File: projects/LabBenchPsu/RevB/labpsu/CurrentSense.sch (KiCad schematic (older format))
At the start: 24 parts

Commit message: working on schematic
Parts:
- added C21: 100nF, symbol C
- added R36: 1K, symbol R
- gave numbers to parts that had none: 23
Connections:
- net CurrentSense: now also C21.1, R36.1; no longer IC2.7 (OUT), R35.1
- net GND: now also C21.2
- new net: IC2.7 (OUT), R35.1, R36.2
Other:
- note added: "1mV / 1mA"
- note added: "Currents up to 320mA can be measured with high\nprecision through the INA219. For higher currents\nthe semi-precisese differential amplifier can be used."
- note added: "Differential amplifier high-side current sensor"
- note added: "differential amplifier"
- note added: "voltage follower"

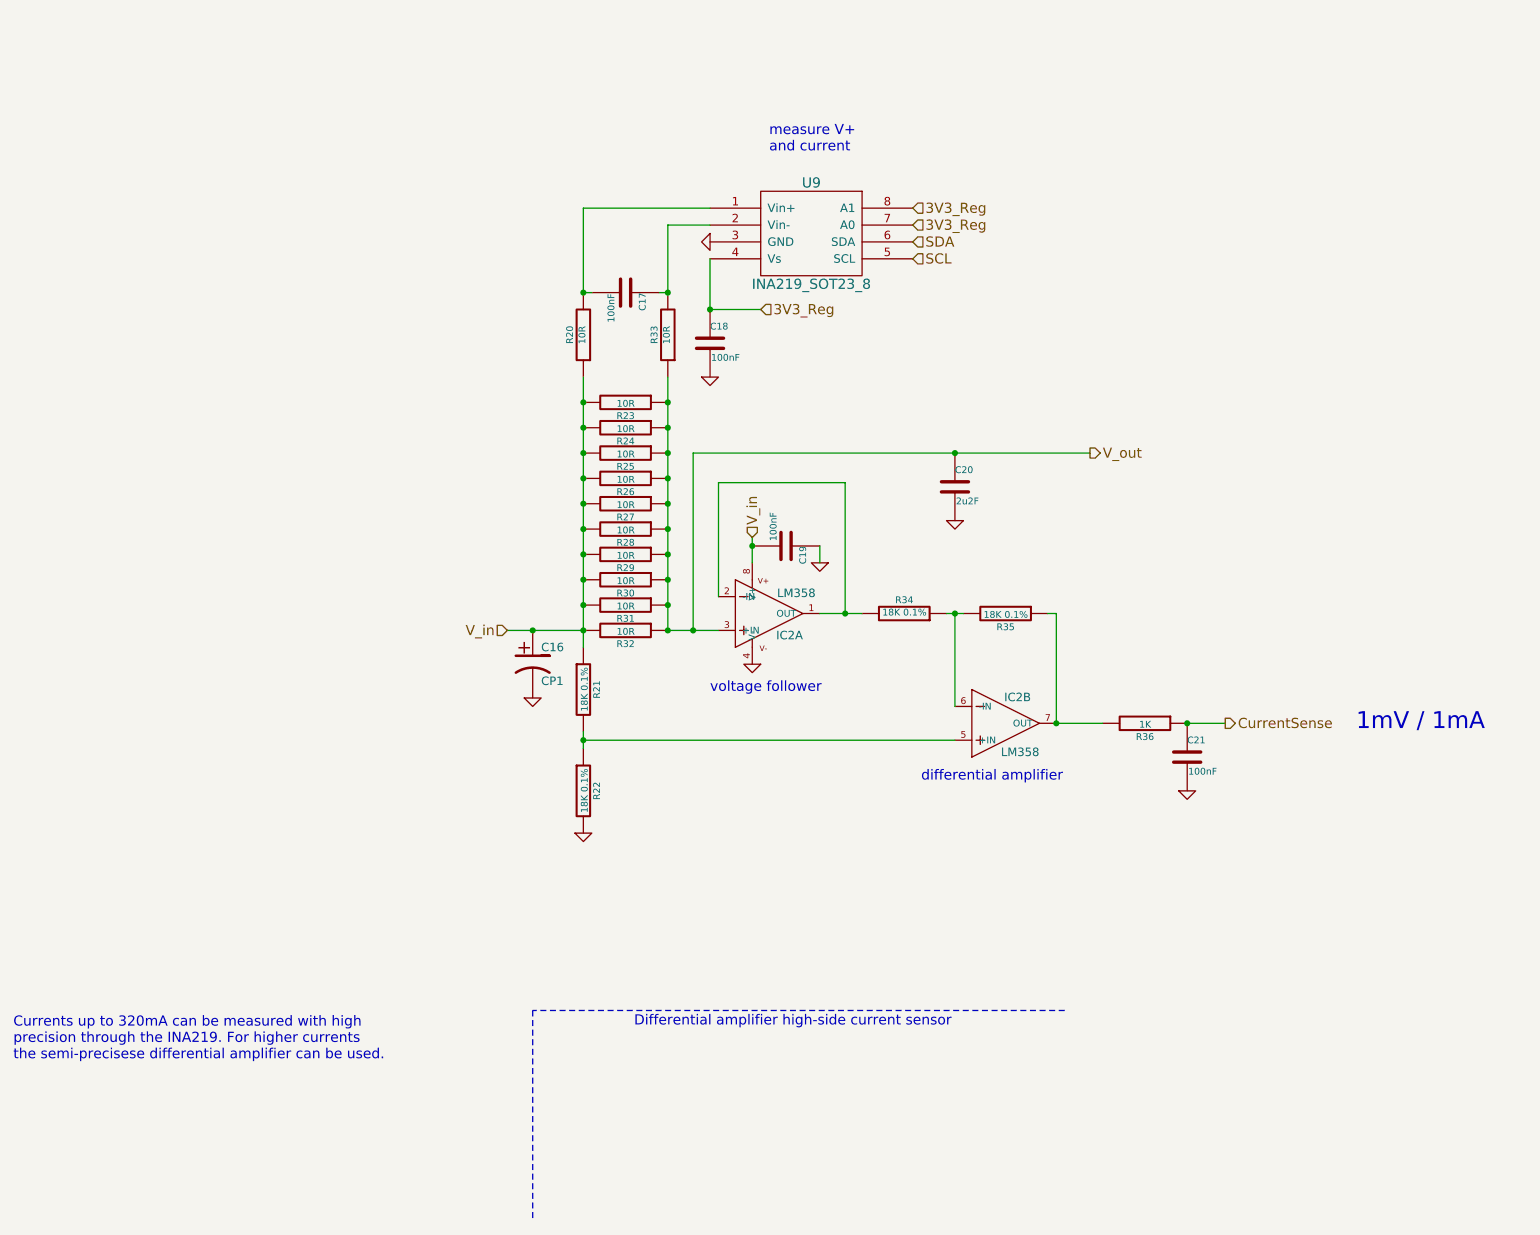
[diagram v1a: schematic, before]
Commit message: redraw schematic
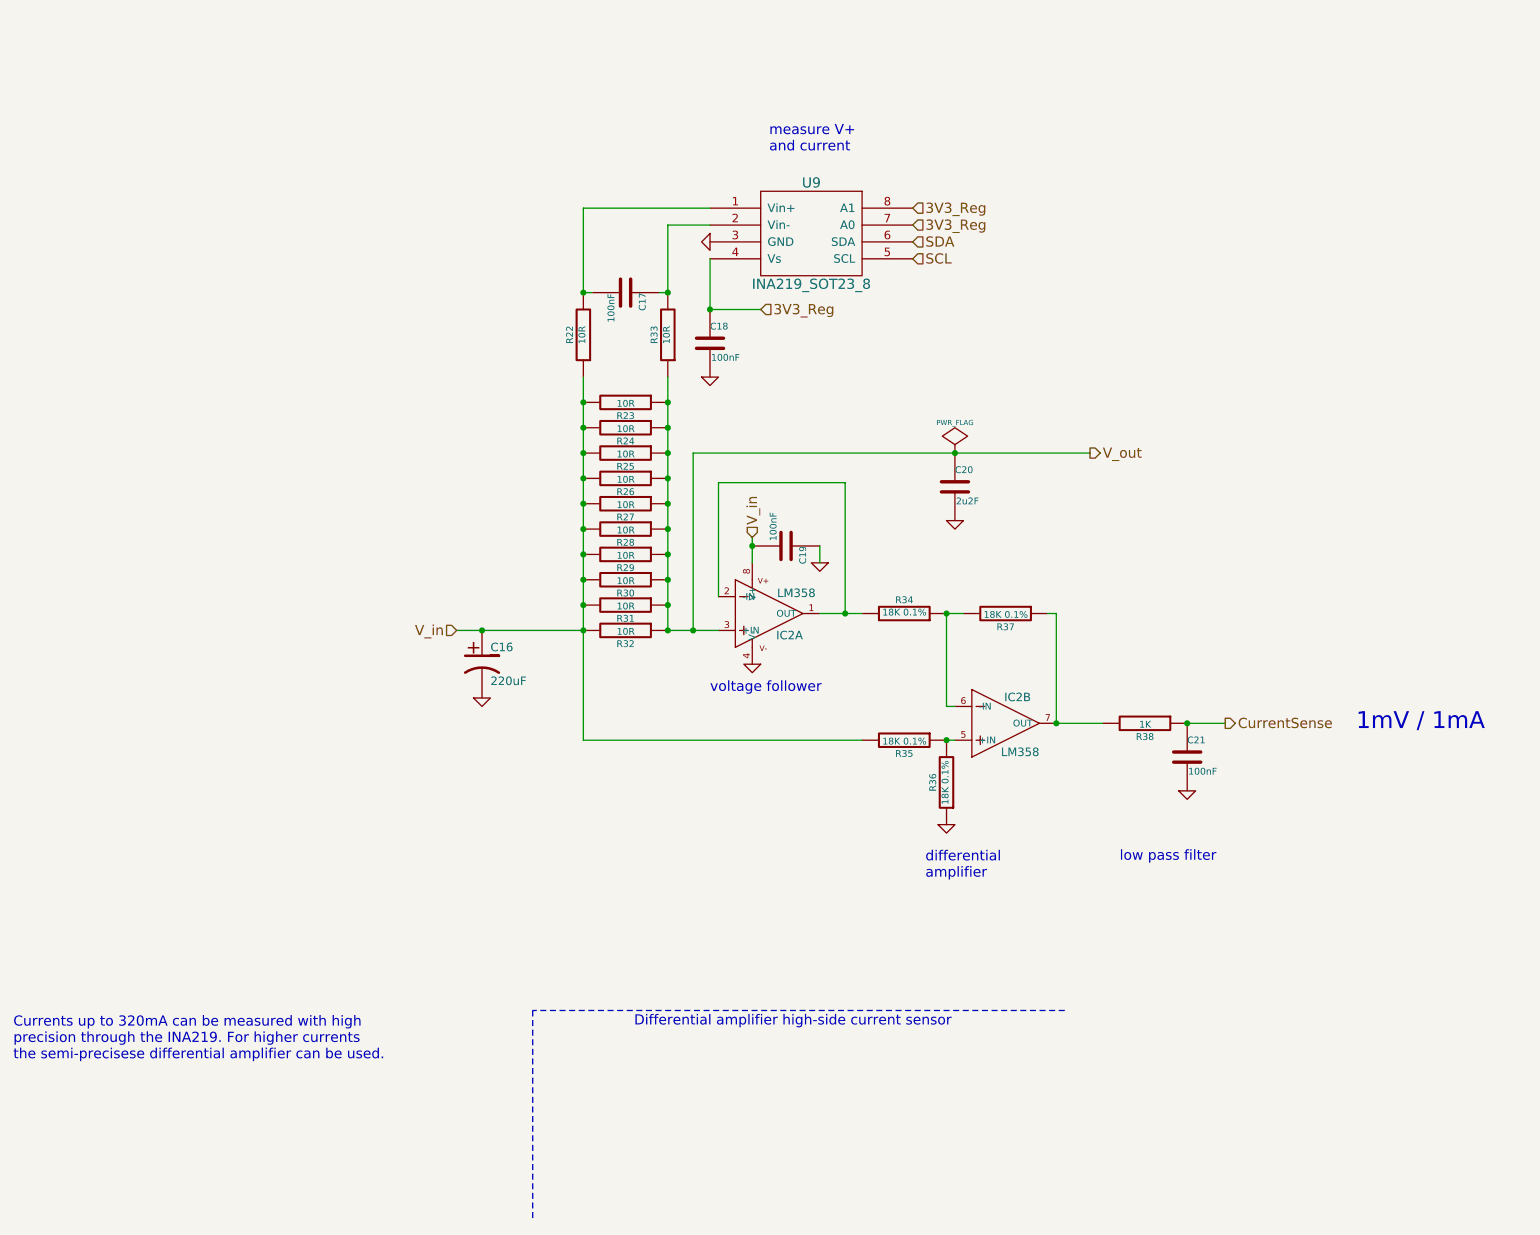
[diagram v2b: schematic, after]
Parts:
- C16: value CP1 -> 220uF
- renumbered R20 to R22, R21 to R35, R22 to R36, R35 to R37, R36 to R38
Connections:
- net GND: now also R36.1; no longer R36.2
- net V_in: now also R35.2; no longer R35.1
- new net: IC2.5 (+IN), R35.1, R36.2
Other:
- note added: "differential \namplifier"
- note added: "low pass filter"
- note removed: "differential amplifier"
- moved on the sheet: C16, R35, R36
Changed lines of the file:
@@
 $Descr A4 11693 8268
 encoding utf-8
-Sheet 3 3
+Sheet 2 3
 Title "Lab Psu (0-20V 0-2A)"
 Date ""
@@
 L CP1 C16
 U 1 1 57DE3B6C
-P 3800 4475
-F 0 "C16" H 3850 4575 50  0000 L CNN
-F 1 "CP1" H 3850 4375 50  0000 L CNN
-F 2 "" H 3800 4475 60  0000 C CNN
-F 3 "" H 3800 4475 60  0000 C CNN
-	1    3800 4475
+P 3500 4475
+F 0 "C16" H 3550 4575 50  0000 L CNN
+F 1 "220uF" H 3550 4375 50  0000 L CNN
+F 2 "" H 3500 4475 60  0000 C CNN
+F 3 "" H 3500 4475 60  0000 C CNN
+	1    3500 4475
 	1    0    0    -1
 $EndComp
 $Comp
-L GND #PWR037
+L GND #PWR024
 U 1 1 57DE3B73
-P 3800 4675
-F 0 "#PWR037" H 3800 4675 30  0001 C CNN
-F 1 "GND" H 3800 4605 30  0001 C CNN
-F 2 "" H 3800 4675 60  0000 C CNN
-F 3 "" H 3800 4675 60  0000 C CNN
-	1    3800 4675
+P 3500 4675
+F 0 "#PWR024" H 3500 4675 30  0001 C CNN
+F 1 "GND" H 3500 4605 30  0001 C CNN
+F 2 "" H 3500 4675 60  0000 C CNN
+F 3 "" H 3500 4675 60  0000 C CNN
+	1    3500 4675
 	1    0    0    -1
 $EndComp
@@
 $EndComp
 $Comp
-L R R20
+L R R22
 U 1 1 57DE3BBF
 P 4100 2525
-F 0 "R20" V 4180 2525 40  0000 C CNN
+F 0 "R22" V 4180 2525 40  0000 C CNN
 F 1 "10R" V 4107 2526 40  0000 C CNN
 F 2 "" V 4030 2525 30  0000 C CNN
@@
 $EndComp
 $Comp
-L GND #PWR038
+L GND #PWR025
 U 1 1 57DE3BDC
 P 4850 1975
-F 0 "#PWR038" H 4850 1975 30  0001 C CNN
+F 0 "#PWR025" H 4850 1975 30  0001 C CNN
 F 1 "GND" H 4850 1905 30  0001 C CNN
 F 2 "" H 4850 1975 60  0000 C CNN
@@
 Connection ~ 4600 2275
 Wire Wire Line
-	4100 2775 4100 4375
+	4100 2775 4100 4925
 Connection ~ 4100 2925
 Connection ~ 4100 3075
@@
 $EndComp
 $Comp
-L GND #PWR039
+L GND #PWR026
 U 1 1 57DE3C08
 P 4850 2775
-F 0 "#PWR039" H 4850 2775 30  0001 C CNN
+F 0 "#PWR026" H 4850 2775 30  0001 C CNN
 F 1 "GND" H 4850 2705 30  0001 C CNN
 F 2 "" H 4850 2775 60  0000 C CNN
@@
 $EndComp
 $Comp
-L GND #PWR040
+L GND #PWR027
 U 1 1 57DE3C22
 P 5100 4475
-F 0 "#PWR040" H 5100 4475 30  0001 C CNN
+F 0 "#PWR027" H 5100 4475 30  0001 C CNN
 F 1 "GND" H 5100 4405 30  0001 C CNN
 F 2 "" H 5100 4475 60  0000 C CNN
@@
 	4900 3400 4900 4075
 Wire Wire Line
-	3650 4275 4100 4275
-Connection ~ 3800 4275
+	3350 4275 4100 4275
+Connection ~ 3500 4275
 Wire Wire Line
 	4600 4275 4900 4275
@@
 Connection ~ 4100 4275
 $Comp
-L R R21
+L R R35
 U 1 1 57DE3C2E
-P 4100 4625
-F 0 "R21" V 4180 4625 40  0000 C CNN
-F 1 "18K 0.1%" V 4107 4626 40  0000 C CNN
-F 2 "" V 4030 4625 30  0000 C CNN
-F 3 "" H 4100 4625 30  0000 C CNN
-	1    4100 4625
-	1    0    0    -1
-$EndComp
-$Comp
-L R R22
+P 6000 4925
+F 0 "R35" V 6080 4925 40  0000 C CNN
+F 1 "18K 0.1%" V 6007 4926 40  0000 C CNN
+F 2 "" V 5930 4925 30  0000 C CNN
+F 3 "" H 6000 4925 30  0000 C CNN
+	1    6000 4925
+	0    1    1    0
+$EndComp
+$Comp
+L R R36
 U 1 1 57DE3C35
-P 4100 5225
-F 0 "R22" V 4180 5225 40  0000 C CNN
-F 1 "18K 0.1%" V 4107 5226 40  0000 C CNN
-F 2 "" V 4030 5225 30  0000 C CNN
-F 3 "" H 4100 5225 30  0000 C CNN
-	1    4100 5225
-	1    0    0    -1
-$EndComp
-$Comp
-L R R35
+P 6250 5175
+F 0 "R36" V 6330 5175 40  0000 C CNN
+F 1 "18K 0.1%" V 6257 5176 40  0000 C CNN
+F 2 "" V 6180 5175 30  0000 C CNN
+F 3 "" H 6250 5175 30  0000 C CNN
+	1    6250 5175
+	-1   0    0    1
+$EndComp
+$Comp
+L R R37
 U 1 1 57DE3C3C
 P 6600 4175
-F 0 "R35" V 6680 4175 40  0000 C CNN
+F 0 "R37" V 6680 4175 40  0000 C CNN
 F 1 "18K 0.1%" V 6607 4176 40  0000 C CNN
 F 2 "" V 6530 4175 30  0000 C CNN
@@
 $EndComp
 $Comp
-L GND #PWR041
+L GND #PWR028
 U 1 1 57DE3C4A
-P 4100 5475
-F 0 "#PWR041" H 4100 5475 30  0001 C CNN
-F 1 "GND" H 4100 5405 30  0001 C CNN
-F 2 "" H 4100 5475 60  0000 C CNN
-F 3 "" H 4100 5475 60  0000 C CNN
-	1    4100 5475
+P 6250 5425
+F 0 "#PWR028" H 6250 5425 30  0001 C CNN
+F 1 "GND" H 6250 5355 30  0001 C CNN
+F 2 "" H 6250 5425 60  0000 C CNN
+F 3 "" H 6250 5425 60  0000 C CNN
+	1    6250 5425
 	1    0    0    -1
 $EndComp
 Wire Wire Line
-	4100 4875 4100 4975
-Wire Wire Line
-	6300 4175 6300 4725
-Wire Wire Line
-	4100 4925 6300 4925
-Connection ~ 4100 4925
-Wire Wire Line
 	6250 4175 6350 4175
-Connection ~ 6300 4175
 $Comp
 L C C19
@@
 $EndComp
 $Comp
-L GND #PWR042
+L GND #PWR029
 U 1 1 57DE3C5D
 P 5500 3875
-F 0 "#PWR042" H 5500 3875 30  0001 C CNN
+F 0 "#PWR029" H 5500 3875 30  0001 C CNN
 F 1 "GND" H 5500 3805 30  0001 C CNN
 F 2 "" H 5500 3875 60  0000 C CNN
@@
 $EndComp
 $Comp
-L GND #PWR043
+L GND #PWR030
 U 1 1 57DE3C73
 P 6300 3625
-F 0 "#PWR043" H 6300 3625 30  0001 C CNN
+F 0 "#PWR030" H 6300 3625 30  0001 C CNN
 F 1 "GND" H 6300 3555 30  0001 C CNN
 F 2 "" H 6300 3625 60  0000 C CNN
@@
 Wire Wire Line
 	4750 3225 7100 3225
-Text HLabel 3650 4275 0    60   Input ~ 0
+Text HLabel 3350 4275 0    60   Input ~ 0
 V_in
 Text HLabel 7100 3225 2    60   Output ~ 0
@@
 Data
 89 50 4E 47 0D 0A 1A 0A 00 00 00 0D 49 48 44 52 00 00 01 5A 00 00 00 99 08 02 00 00 00 E1 38 65
-8F 00 00 00 03 73 42 49 54 08 08 08 DB E1 4F E0 00 00 00 09 70 48 59 73 00 00 0F 61 00 00 0F 61
-01 A8 3F A7 69 00 00 20 00 49 44 41 54 78 9C ED BD 7F 7C 54 D5 99 3F FE 3C 67 50 41 99 99 E8 77
+8F 00 00 00 03 73 42 49 54 08 08 08 DB E1 4F E0 00 00 00 09 70 48 59 73 00 00 0F 3C 00 00 0F 3C
+01 17 3A 9F 59 00 00 20 00 49 44 41 54 78 9C ED BD 7F 7C 54 D5 99 3F FE 3C 67 50 41 99 99 E8 77
 B7 B6 64 42 08 B6 EA 04 05 DA AD 99 89 35 C1 6E 33 93 DD 82 EE 36 33 28 01 51 13 0A C1 4A 7E 58
 33 D8 96 04 2B 89 DD 36 89 32 13 6C 15 2A 09 82 12 94 99 A0 08 5D 93 60 2B A0 66 26 EE 6E C1 CA
@@
 2D 9F 88 43 F3 3C 90 4C 6B C8 18 4B 68 82 1D D5 96 C4 7C 82 71 B8 96 C4 37 29 96 16 40 D4 66 21
 05 72 8C 5F EE 20 A9 93 89 02 05 17 06 65 2C 25 C3 F8 25 07 0A 14 28 B8 C8 F8 FF 01 C8 83 A7 59
-65 DF 99 A4 00 00 00 00 49 45 4E 44 AE 42 60 82 EC
+65 DF 99 A4 00 00 00 00 49 45 4E 44 AE 42 60 82 88
 EndData
 $EndBitmap
 Text Notes 4400 6625 0    60   ~ 0
 Differential amplifier high-side current sensor
-Text Notes 6100 5175 0    60   ~ 0
-differential amplifier
+Text Notes 6125 5750 0    60   ~ 0
+differential \namplifier
 Text Notes 8675 4875 0    100  ~ 0
 1mV / 1mA
@@
 $EndComp
 $Comp
-L R R36
+L R R38
 U 1 1 57E047E2
 P 7425 4825
-F 0 "R36" V 7505 4825 40  0000 C CNN
+F 0 "R38" V 7505 4825 40  0000 C CNN
 F 1 "1K" V 7432 4826 40  0000 C CNN
 F 2 "" V 7355 4825 30  0000 C CNN
@@
 $EndComp
 $Comp
-L GND #PWR044
+L GND #PWR031
 U 1 1 57E047E9
 P 7675 5225
-F 0 "#PWR044" H 7675 5225 30  0001 C CNN
+F 0 "#PWR031" H 7675 5225 30  0001 C CNN
 F 1 "GND" H 7675 5155 30  0001 C CNN
 F 2 "" H 7675 5225 60  0000 C CNN
@@
 Text Notes 725  6825 0    60   ~ 0
 Currents up to 320mA can be measured with high\nprecision through the INA219. For higher currents\nthe semi-precisese differential amplifier can be used.
+Wire Wire Line
+	6250 4925 6300 4925
+Wire Wire Line
+	4100 4925 5750 4925
+Connection ~ 6250 4925
+Wire Wire Line
+	6300 4725 6250 4725
+Wire Wire Line
+	6250 4725 6250 4175
+Connection ~ 6250 4175
+Text Notes 7275 5650 0    60   ~ 0
+low pass filter
+$Comp
+L PWR_FLAG #FLG032
+U 1 1 57E1B1A8
+P 6300 3225
+F 0 "#FLG032" H 6300 3320 30  0001 C CNN
+F 1 "PWR_FLAG" H 6300 3405 30  0000 C CNN
+F 2 "" H 6300 3225 60  0000 C CNN
+F 3 "" H 6300 3225 60  0000 C CNN
+	1    6300 3225
+	1    0    0    -1
+$EndComp
 $EndSCHEMATC

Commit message: schematic more or less done
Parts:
- IC1: renamed from IC2; footprint SparkFun-SO08 -> (none)
- renumbered C19 to C10, C20 to C11, C21 to C12, C16 to C7, C17 to C8, C18 to C9, R23 to R10, R24 to R11, R25 to R12, R26 to R13, R27 to R14, R28 to R15, R29 to R16, R30 to R17, R31 to R18, R32 to R19, R33 to R20, R34 to R21, R35 to R22, R36 to R23, R37 to R24, R38 to R25, R22 to R9, U9 to U5

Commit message: schematic reviewed
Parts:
- removed U5: INA219_SOT23_8, symbol INA219_SOT23_8
- added U5: INA219, symbol INA219
- R10, R11, R12, R13, R14, R15, R16, R17, R18, R19: value 10R -> 10R 1%
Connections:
- net 3V3_Reg: now also U5.1 (A1), U5.2 (A0), U5.5 (Vs)
- net GND: now also U5.6 (GND)
- net SCL: now also U5.4 (SCL)
- net SDA: now also U5.3 (SDA)
- net at C8.2, R9.2: now also U5.8 (Vin+)
- net at C8.1, R20.2: now also U5.7 (Vin-)
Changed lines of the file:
@@
 P 4350 4125
 F 0 "R18" V 4430 4125 40  0000 C CNN
-F 1 "10R" V 4357 4126 40  0000 C CNN
+F 1 "10R 1%" V 4357 4126 40  0000 C CNN
 F 2 "" V 4280 4125 30  0001 C CNN
 F 3 "" H 4350 4125 30  0000 C CNN
@@
 P 4350 3975
 F 0 "R17" V 4430 3975 40  0000 C CNN
-F 1 "10R" V 4357 3976 40  0000 C CNN
+F 1 "10R 1%" V 4357 3976 40  0000 C CNN
 F 2 "" V 4280 3975 30  0001 C CNN
 F 3 "" H 4350 3975 30  0000 C CNN
@@
 P 4350 3825
 F 0 "R16" V 4430 3825 40  0000 C CNN
-F 1 "10R" V 4357 3826 40  0000 C CNN
+F 1 "10R 1%" V 4357 3826 40  0000 C CNN
 F 2 "" V 4280 3825 30  0001 C CNN
 F 3 "" H 4350 3825 30  0000 C CNN
@@
 P 4350 3675
 F 0 "R15" V 4430 3675 40  0000 C CNN
-F 1 "10R" V 4357 3676 40  0000 C CNN
+F 1 "10R 1%" V 4357 3676 40  0000 C CNN
 F 2 "" V 4280 3675 30  0001 C CNN
 F 3 "" H 4350 3675 30  0000 C CNN
@@
 P 4350 4275
 F 0 "R19" V 4430 4275 40  0000 C CNN
-F 1 "10R" V 4357 4276 40  0000 C CNN
+F 1 "10R 1%" V 4357 4276 40  0000 C CNN
 F 2 "" V 4280 4275 30  0001 C CNN
 F 3 "" H 4350 4275 30  0000 C CNN
@@
 P 4350 3375
 F 0 "R13" V 4430 3375 40  0000 C CNN
-F 1 "10R" V 4357 3376 40  0000 C CNN
+F 1 "10R 1%" V 4357 3376 40  0000 C CNN
 F 2 "" V 4280 3375 30  0001 C CNN
 F 3 "" H 4350 3375 30  0000 C CNN
@@
 P 4350 3225
 F 0 "R12" V 4430 3225 40  0000 C CNN
-F 1 "10R" V 4357 3226 40  0000 C CNN
+F 1 "10R 1%" V 4357 3226 40  0000 C CNN
 F 2 "" V 4280 3225 30  0001 C CNN
 F 3 "" H 4350 3225 30  0000 C CNN
@@
 P 4350 3075
 F 0 "R11" V 4430 3075 40  0000 C CNN
-F 1 "10R" V 4357 3076 40  0000 C CNN
+F 1 "10R 1%" V 4357 3076 40  0000 C CNN
 F 2 "" V 4280 3075 30  0001 C CNN
 F 3 "" H 4350 3075 30  0000 C CNN
@@
 P 4350 2925
 F 0 "R10" V 4430 2925 40  0000 C CNN
-F 1 "10R" V 4357 2926 40  0000 C CNN
+F 1 "10R 1%" V 4357 2926 40  0000 C CNN
 F 2 "" V 4280 2925 30  0001 C CNN
 F 3 "" H 4350 2925 30  0000 C CNN
@@
 P 4350 3525
 F 0 "R14" V 4430 3525 40  0000 C CNN
-F 1 "10R" V 4357 3526 40  0000 C CNN
+F 1 "10R 1%" V 4357 3526 40  0000 C CNN
 F 2 "" V 4280 3525 30  0001 C CNN
 F 3 "" H 4350 3525 30  0000 C CNN
@@
 	1    4350 2275
 	0    1    1    0
-$EndComp
-$Comp
-L INA219_SOT23_8 U5
-U 1 1 57DE3BD4
-P 5450 1925
-F 0 "U5" H 5450 2225 60  0000 C CNN
-F 1 "INA219_SOT23_8" H 5450 1625 60  0000 C CNN
-F 2 "" H 5450 1725 60  0001 C CNN
-F 3 "" H 5450 1725 60  0000 C CNN
-	1    5450 1925
-	-1   0    0    -1
 $EndComp
 $Comp
@@
 	1    0    0    -1
 $EndComp
+$Comp
+L INA219 U5
+U 1 1 581847C5
+P 5450 1925
+F 0 "U5" H 5450 2225 60  0000 C CNN
+F 1 "INA219" H 5450 1625 60  0000 C CNN
+F 2 "" H 5450 1725 60  0000 C CNN
+F 3 "" H 5450 1725 60  0000 C CNN
+	1    5450 1925
+	-1   0    0    -1
+$EndComp
 $EndSCHEMATC
